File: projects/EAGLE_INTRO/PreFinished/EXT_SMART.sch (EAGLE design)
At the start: 5 parts

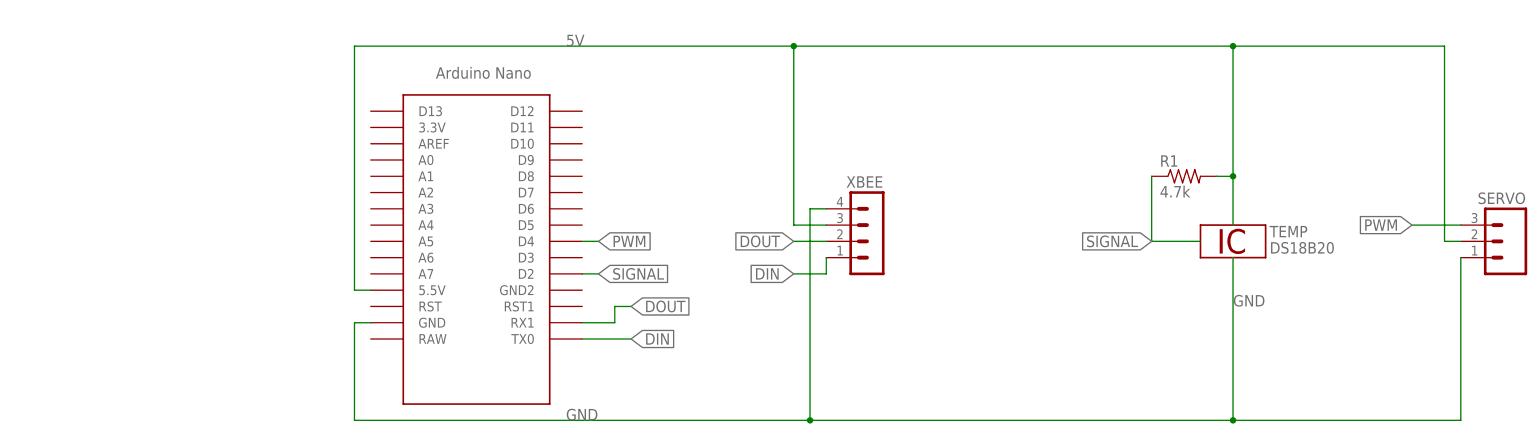
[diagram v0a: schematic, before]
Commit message: Added edits to teensy 3.6 schematic for the plantower. Added stuff from EAGLE intro presentation.
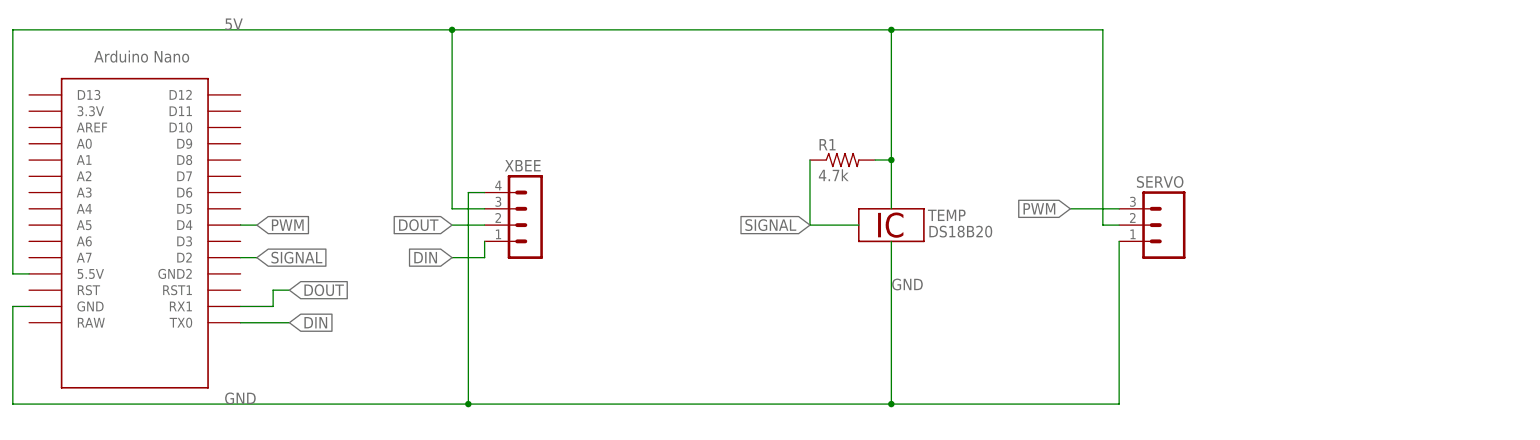
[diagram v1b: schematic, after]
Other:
- moved on the sheet: R1, SERVO, TEMP, XBEE
